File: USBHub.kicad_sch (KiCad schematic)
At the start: 3 parts, among them CN1 UE27BC54130, CN2 UE27AC54100, CN3 UE27AC54100

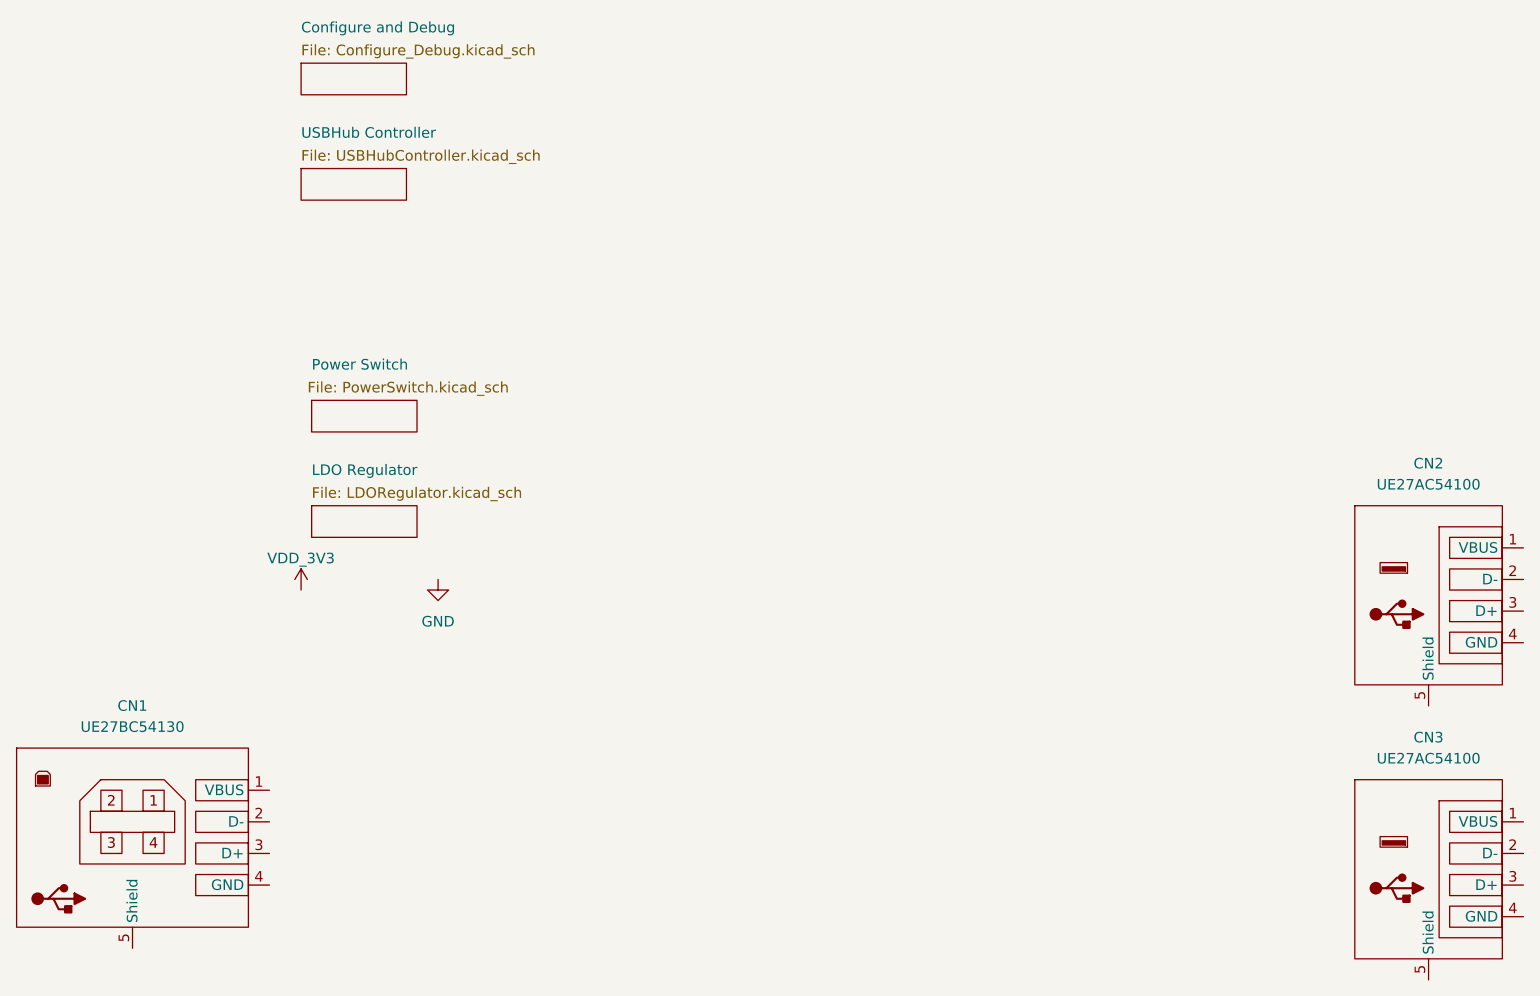
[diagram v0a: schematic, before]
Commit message: 更换电阻至新的结构
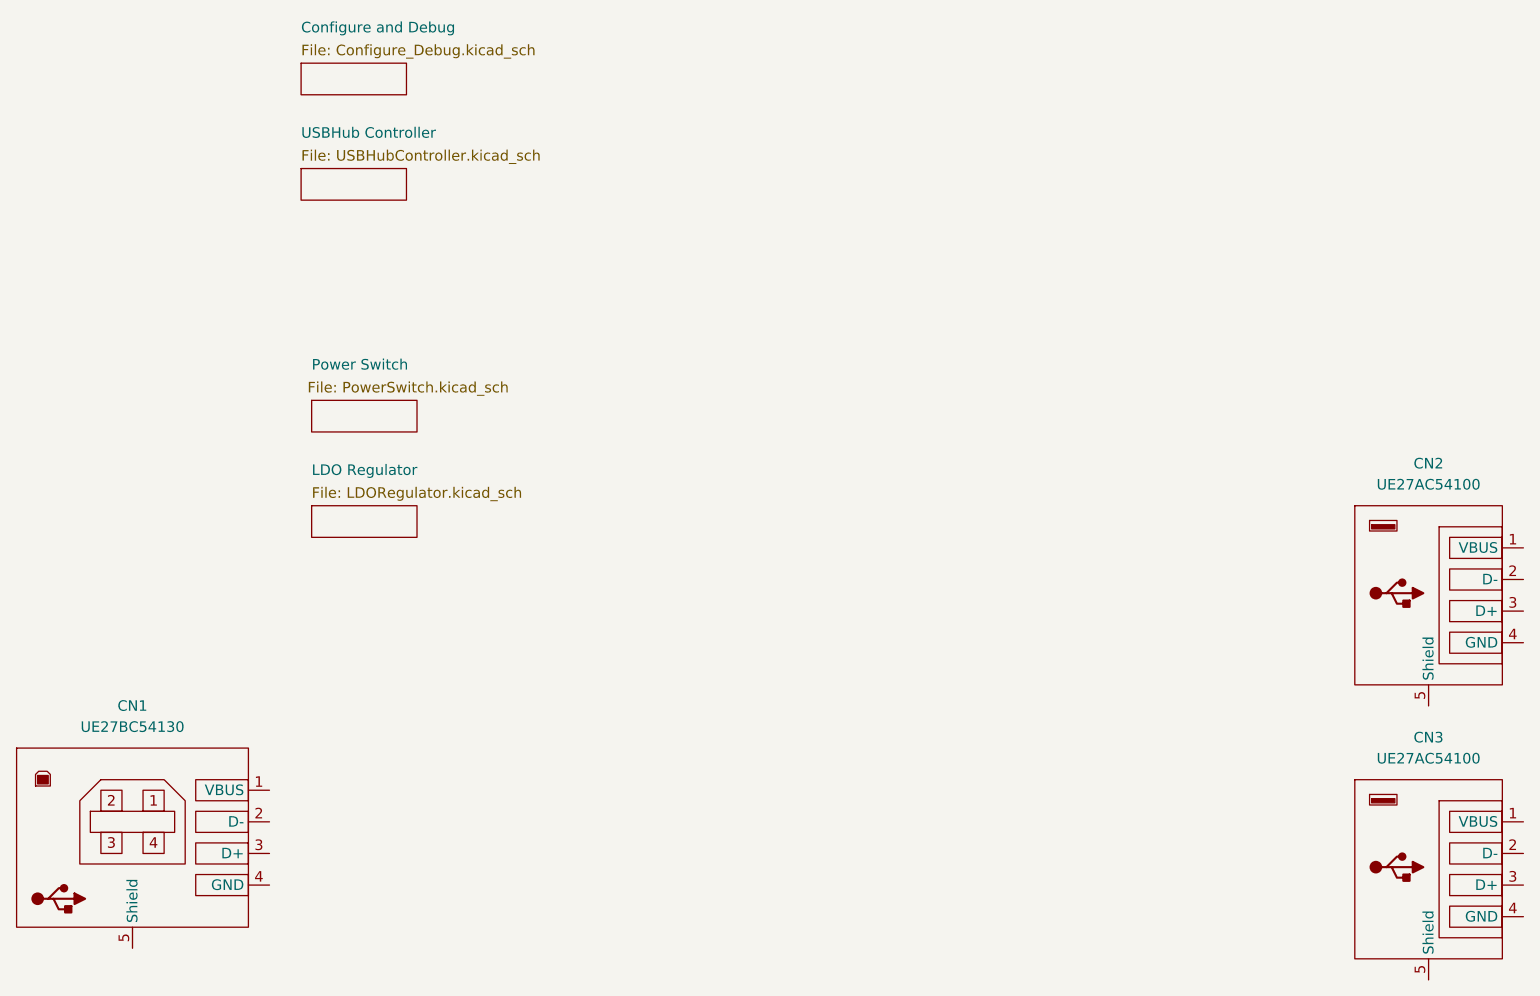
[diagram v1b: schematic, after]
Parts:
- CN1: footprint MY_Connector_USB:UE27BC54130 -> MY_Connector_USB:Amphenol_UE27BC54130; 详细描述 (none) -> USB-B（USB TYPE-B） USB 2.0 插座 连接器 4 位 通孔，直角
- CN2, CN3: footprint MY_Connector_USB:UE27AC54100 -> MY_Connector_USB:Amphenol_UE27AC54100; MPN (none) -> UE27AC54100; Manufacturer (none) -> Amphenol Canada Corp; 详细描述 (none) -> USB-A（USB TYPE-A） USB 2.0 插座 连接器 4 位 通孔，直角
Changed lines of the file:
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@@
 			)
 		)
-		(property "Footprint" "MY_Connector_USB:UE27AC54100"
+		(property "Footprint" "MY_Connector_USB:Amphenol_UE27AC54100"
 			(at 208.28 112.268 0)
 			(effects
@@
 			)
 		)
-		(property "Datasheet" "https://cdn.amphenol-cs.com/media/wysiwyg/files/drawing/pue27acx4x0x.pdf"
+		(property "Datasheet" "kicad-embed://pue27acx4x0x.pdf"
 			(at 208.28 116.332 0)
 			(effects
@@
 			)
 		)
-		(property "Description" "USB-A（USB TYPE-A） USB 2.0 插座 连接器 4 位 通孔，直角"
+		(property "Description" "USB-A（USB TYPE-A）连接器  CONN RCPT USB2.0 TYPEA 4POS R/A"
 			(at 208.28 114.3 0)
+			(effects
+				(font
+					(size 1.27 1.27)
+				)
+				(hide yes)
+			)
+		)
+		(property "MPN" "UE27AC54100"
+			(at 208.28 115.824 0)
+			(effects
+				(font
+					(size 1.27 1.27)
+				)
+				(hide yes)
+			)
+		)
+		(property "Manufacturer" "Amphenol Canada Corp"
+			(at 208.28 117.856 0)
+			(effects
+				(font
+					(size 1.27 1.27)
+				)
+				(hide yes)
+			)
+		)
+		(property "详细描述" "USB-A（USB TYPE-A） USB 2.0 插座 连接器 4 位 通孔，直角"
+			(at 208.28 124.206 0)
 			(effects
 				(font
@@
 			)
 		)
-		(property "Footprint" "MY_Connector_USB:UE27AC54100"
+		(property "Footprint" "MY_Connector_USB:Amphenol_UE27AC54100"
 			(at 208.28 145.288 0)
 			(effects
@@
 			)
 		)
-		(property "Datasheet" "https://cdn.amphenol-cs.com/media/wysiwyg/files/drawing/pue27acx4x0x.pdf"
+		(property "Datasheet" "kicad-embed://pue27acx4x0x.pdf"
 			(at 208.28 149.352 0)
 			(effects
@@
 			)
 		)
-		(property "Description" "USB-A（USB TYPE-A） USB 2.0 插座 连接器 4 位 通孔，直角"
+		(property "Description" "USB-A（USB TYPE-A）连接器  CONN RCPT USB2.0 TYPEA 4POS R/A"
 			(at 208.28 147.32 0)
+			(effects
+				(font
+					(size 1.27 1.27)
+				)
+				(hide yes)
+			)
+		)
+		(property "MPN" "UE27AC54100"
+			(at 208.28 148.844 0)
+			(effects
+				(font
+					(size 1.27 1.27)
+				)
+				(hide yes)
+			)
+		)
+		(property "Manufacturer" "Amphenol Canada Corp"
+			(at 208.28 150.876 0)
+			(effects
+				(font
+					(size 1.27 1.27)
+				)
+				(hide yes)
+			)
+		)
+		(property "详细描述" "USB-A（USB TYPE-A） USB 2.0 插座 连接器 4 位 通孔，直角"
+			(at 208.28 157.226 0)
 			(effects
 				(font
@@
 				(path "/07e28d9d-adcb-473d-a362-1ef0c979820d"
 					(reference "CN3")
-					(unit 1)
-				)
-			)
-		)
-	)
-	(symbol
-		(lib_id "power:GND")
-		(at 88.9 87.63 0)
-		(unit 1)
-		(exclude_from_sim no)
-		(in_bom yes)
-		(on_board yes)
-		(dnp no)
-		(fields_autoplaced yes)
-		(property "Reference" "#PWR01"
-			(at 88.9 93.98 0)
-			(effects
-				(font
-					(size 1.27 1.27)
-				)
-				(hide yes)
-			)
-		)
-		(property "Value" "GND"
-			(at 88.9 92.71 0)
-			(effects
-				(font
-					(size 1.27 1.27)
-				)
-			)
-		)
-		(property "Footprint" ""
-			(at 88.9 87.63 0)
-			(effects
-				(font
-					(size 1.27 1.27)
-				)
-				(hide yes)
-			)
-		)
-		(property "Datasheet" ""
-			(at 88.9 87.63 0)
-			(effects
-				(font
-					(size 1.27 1.27)
-				)
-				(hide yes)
-			)
-		)
-		(property "Description" "Power symbol creates a global label with name \"GND\" , ground"
-			(at 88.9 87.63 0)
-			(effects
-				(font
-					(size 1.27 1.27)
-				)
-				(hide yes)
-			)
-		)
-		(pin "1"
-		)
-		(instances
-			(project ""
-				(path "/07e28d9d-adcb-473d-a362-1ef0c979820d"
-					(reference "#PWR01")
 					(unit 1)
 				)
@@
 			)
 		)
-		(property "Footprint" "MY_Connector_USB:UE27BC54130"
+		(property "Footprint" "MY_Connector_USB:Amphenol_UE27BC54130"
 			(at 52.07 140.208 0)
 			(effects
@@
 			)
 		)
-		(property "Datasheet" "https://cdn.amphenol-cs.com/media/wysiwyg/files/drawing/pue27bcx4xxx.pdf"
+		(property "Datasheet" "kicad-embed://pue27bcx4xxx.pdf"
 			(at 52.07 148.082 0)
 			(effects
@@
 			)
 		)
-		(property "Description" "USB 2.0, Type B, Receptacle, Right Angle, 4 Pins, Shell Kink with Nickel Plating, 30μin Gold, Black Housing, with Rear Shield,"
+		(property "Description" "USB-B（USB TYPE-B）连接器 CONN RCPT USB2.0 TYPEB 4POS R/A"
 			(at 52.07 146.05 0)
 			(effects
@@
 		(property "Manufacturer" "Amphenol Canada Corp"
 			(at 52.07 144.018 0)
+			(effects
+				(font
+					(size 1.27 1.27)
+				)
+				(hide yes)
+			)
+		)
+		(property "详细描述" "USB-B（USB TYPE-B） USB 2.0 插座 连接器 4 位 通孔，直角"
+			(at 52.07 152.908 0)
 			(effects
 				(font
@@
 					(unit 1)
 				)
-			)
-		)
-	)
-	(symbol
-		(lib_id "power:VDD")
-		(at 72.39 88.9 0)
-		(unit 1)
-		(exclude_from_sim no)
-		(in_bom yes)
-		(on_board yes)
-		(dnp no)
-		(property "Reference" "#PWR06"
-			(at 72.39 92.71 0)
-			(effects
-				(font
-					(size 1.27 1.27)
-				)
-				(hide yes)
-			)
-		)
-		(property "Value" "VDD_3V3"
-			(at 72.39 85.09 0)
-			(effects
-				(font
-					(size 1.27 1.27)
-				)
-			)
-		)
-		(property "Footprint" ""
-			(at 72.39 88.9 0)
-			(effects
-				(font
-					(size 1.27 1.27)
-				)
-				(hide yes)
-			)
-		)
-		(property "Datasheet" ""
-			(at 72.39 88.9 0)
-			(effects
-				(font
-					(size 1.27 1.27)
-				)
-				(hide yes)
-			)
-		)
-		(property "Description" "Power symbol creates a global label with name \"VDD\""
-			(at 72.39 88.9 0)
-			(effects
-				(font
-					(size 1.27 1.27)
-				)
-				(hide yes)
-			)
-		)
-		(pin "1"
-		)
-		(instances
-			(project "USBHub"
-				(path "/07e28d9d-adcb-473d-a362-1ef0c979820d"
-					(reference "#PWR06")
-					(unit 1)
-				)
